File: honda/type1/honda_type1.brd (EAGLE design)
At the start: 47.8 x 31 mm, 3 parts, among them J1 501645-2620, J2 501645-3620

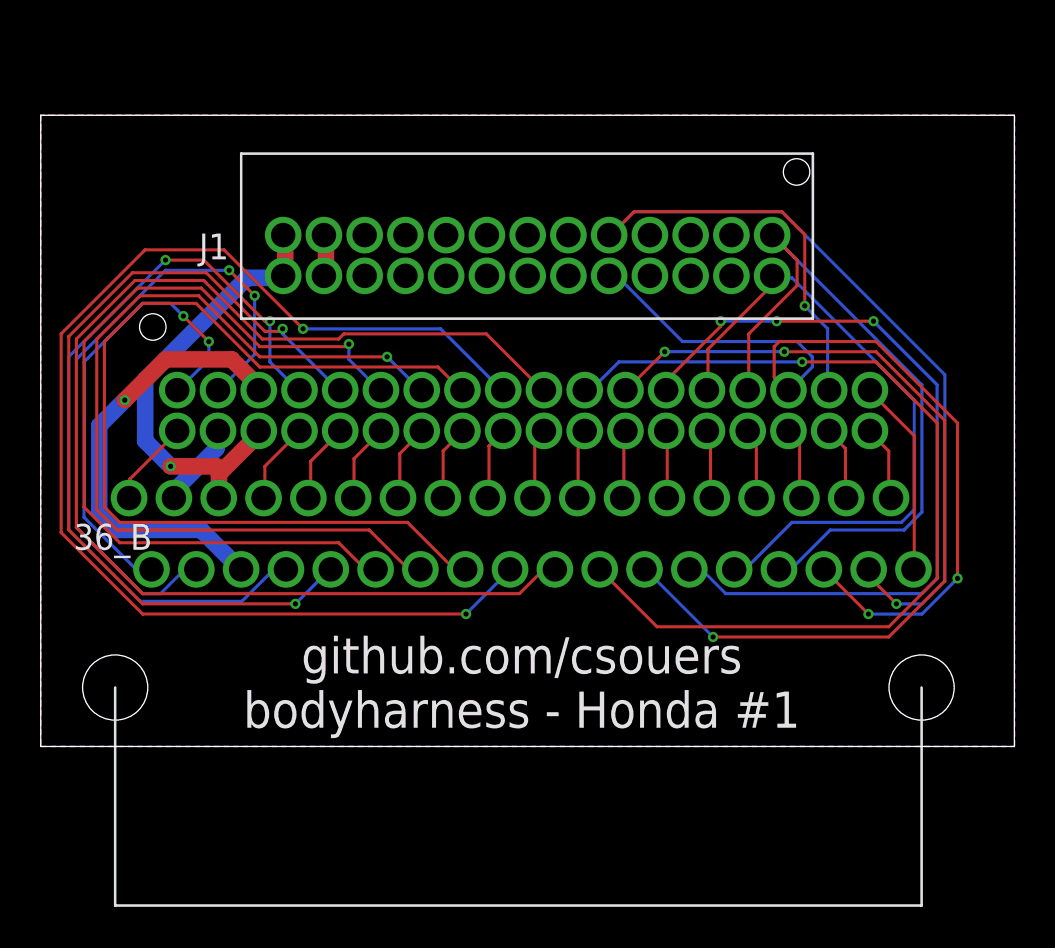
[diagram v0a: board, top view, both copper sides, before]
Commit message: switch to rj45 for the interconnect
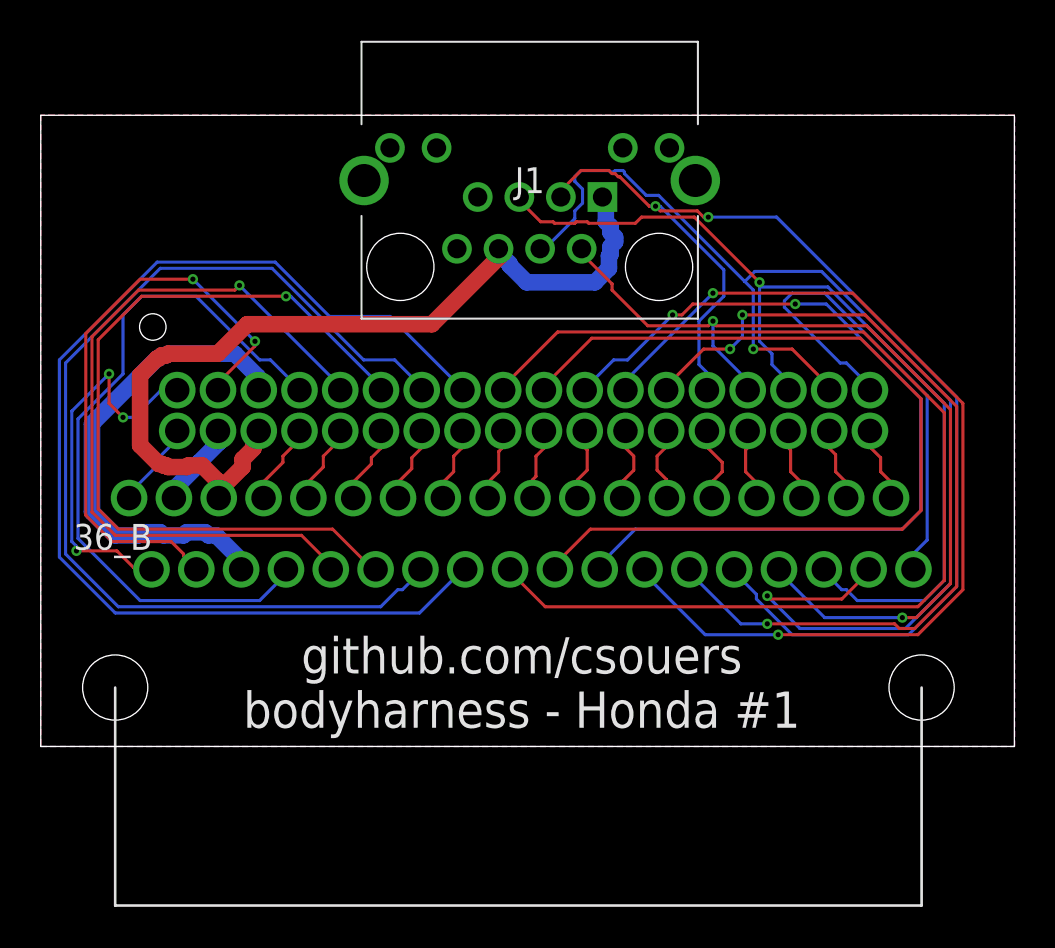
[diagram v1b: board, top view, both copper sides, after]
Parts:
- J1: value 501645-2620 -> RJHSE-3380; device Souers:501645-2620 -> RJHSE-3380:RJHSE3384
- moved J1 8.67 mm to (24.0, 21.0), turned to 0 degrees
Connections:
- removed net AUX2: J1.17
- removed net AUX3: J1.20
- removed net AUX4: J1.19
- removed net CAN1_H: J1.6
- removed net CAN1_L: J1.5
- removed net GMLAN: J1.18
- removed net IGN: J1.23, J1.24
- removed net K_LINE: J1.13
- removed net L_LINE: J1.14
- net CAN0_L: now also J1.3; no longer J1.1
- net CAN2_H: now also J1.4; no longer J1.10
- net CAN2_L: now also J1.5; no longer J1.9
- net GND: no longer J1.11, J1.12, J1.15, J1.16, J1.21, J1.22, J1.3, J1.4
- net VIN: now also J1.1, J1.6; no longer J1.25, J1.26
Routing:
- net CAN0_L: track 31.9 -> 58.8 mm, vias 0 -> 2
- net VIN: track 22.6 -> 43.9 mm, vias 1 -> 0
- net 36B_27: track 61.1 -> 45.7 mm
- net 36B_19: track 9.70 -> 24.4 mm
- net CAN0_H: track 34.0 -> 44.7 mm, vias 0 -> 2
- net 36B_29: track 47.2 -> 56.1 mm
- net CAN2_H: track 54.2 -> 61.9 mm
- net 36B_30: track 44.2 -> 50.7 mm, vias 1 -> 0
- net 36B_25: track 43.0 -> 48.2 mm, vias 3 -> 2
- net 36B_28: track 60.6 -> 55.5 mm, vias 2 -> 0
- net 36B_32: track 41.8 -> 37.1 mm, vias 2 -> 1
- net CAN2_L: track 42.8 -> 47.0 mm, vias 2 -> 1
- net 36B_36: track 23.1 -> 19.2 mm, vias 2 -> 3
- net 36B_24: track 38.9 -> 42.5 mm
- net 36B_33: track 38.4 -> 35.2 mm, vias 2 -> 0
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
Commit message: push
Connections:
- removed net CAN0_H: 36_B.22, J1.2, J2.30
- removed net CAN0_L: 36_B.23, J1.3, J2.28
- new net CAN1_H: 36_B.20, J1.4, J2.34
- new net CAN1_L: 36_B.21, J1.5, J2.32
- net CAN2_H: now also 36_B.22, J1.2, J2.30; no longer 36_B.20, J1.4, J2.34
- net CAN2_L: now also 36_B.23, J1.3, J2.28; no longer 36_B.21, J1.5, J2.32
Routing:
- net CAN1_H: track 0.00 -> 61.9 mm, vias 0 -> 2
- net CAN0_L: track 58.8 -> 0.00 mm, vias 2 -> 0
- net CAN1_L: track 0.00 -> 47.0 mm, vias 0 -> 1
- net CAN0_H: track 44.7 -> 0.00 mm, vias 2 -> 0
- net CAN2_H: track 61.9 -> 44.7 mm
- net CAN2_L: track 47.0 -> 58.8 mm, vias 1 -> 2
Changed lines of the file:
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@@
 <wire x1="22.479" y1="24.384" x2="22.47" y2="24.43" width="0.8128" layer="1"/>
 </signal>
-<signal name="CAN2_H">
+<signal name="CAN1_H">
 <contactref element="36_B" pad="20"/>
 <contactref element="J2" pad="34"/>
@@
 <via x="35.6616" y="7.3914" extent="1-16" drill="0.254"/>
 </signal>
-<signal name="CAN2_L">
+<signal name="CAN1_L">
 <contactref element="36_B" pad="21"/>
 <contactref element="J2" pad="32"/>
@@
 <via x="35.2806" y="22.7838" extent="1-16" drill="0.254"/>
 </signal>
-<signal name="CAN0_H">
+<signal name="CAN2_H">
 <contactref element="36_B" pad="22"/>
 <contactref element="J2" pad="30"/>
@@
 <via x="42.291" y="6.3246" extent="1-16" drill="0.254"/>
 </signal>
-<signal name="CAN0_L">
+<signal name="CAN2_L">
 <contactref element="36_B" pad="23"/>
 <contactref element="J2" pad="28"/>
